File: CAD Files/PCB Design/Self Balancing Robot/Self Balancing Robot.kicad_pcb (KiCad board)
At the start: 2 copper layers, 82.5 x 53 mm, 17 parts, among them J1 Screw_Terminal_01x02, M1 Stepper_Motor_bipolar, M2 Stepper_Motor_bipolar, U1 DEVKIT_V1_ESP32-WROOM-32, U2 TSR_1-2450

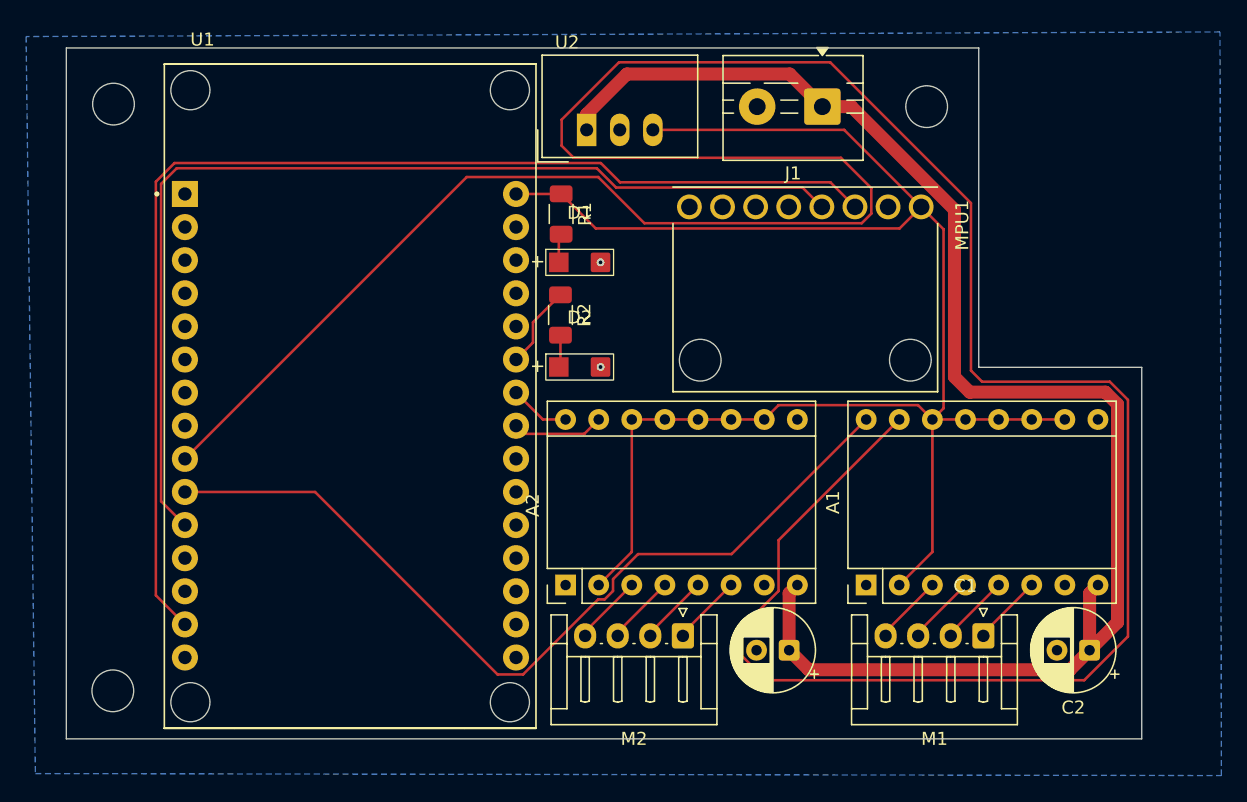
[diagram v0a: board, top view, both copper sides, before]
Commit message: Add 3d models
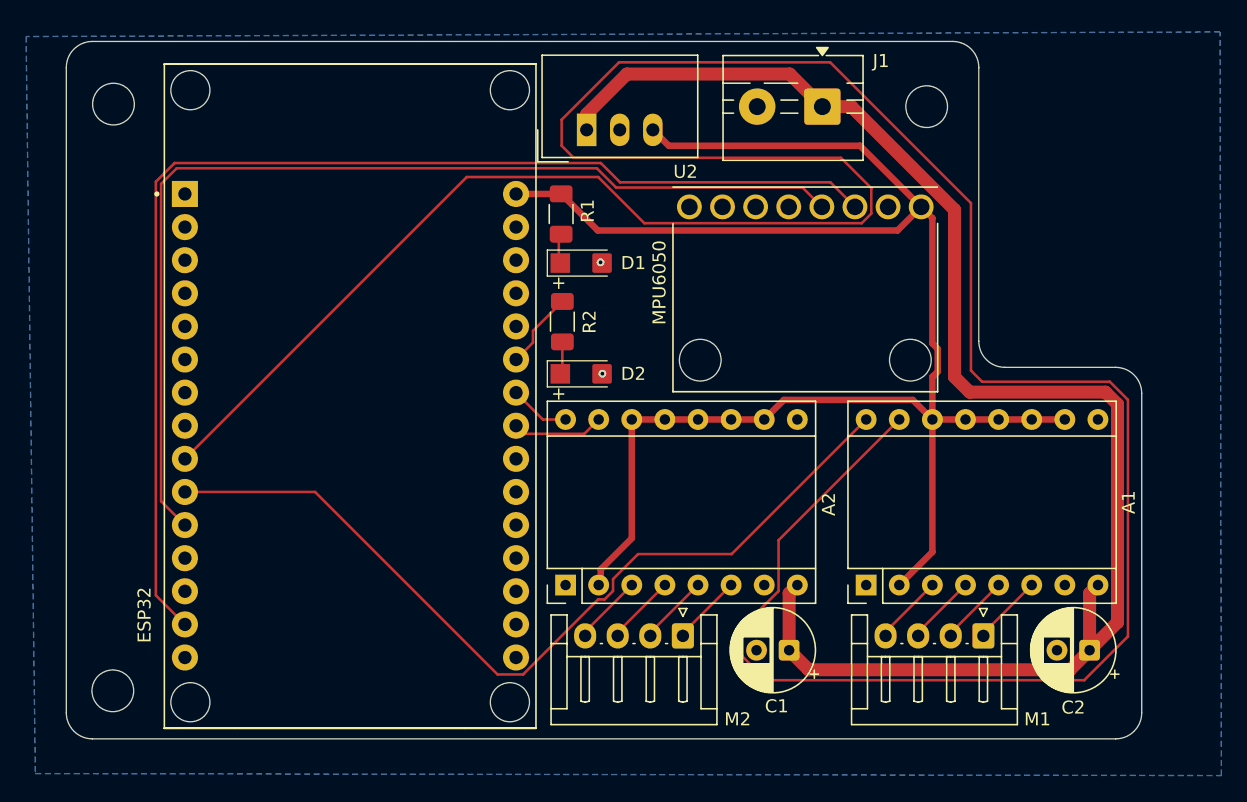
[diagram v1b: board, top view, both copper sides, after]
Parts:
- moved D2 0.54 mm to (126.0, 65.5)
- moved R2 0.53 mm to (124.6, 61.5)
- moved D1 0.13 mm to (126.0, 57.0)
- renumbered U1 to ESP32, MPU1 to MPU6050
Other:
- board size 82.5 x 53 mm -> 82.5 x 53.5 mm

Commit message: Update .gitignore to exclude additional KiCAD temporary files
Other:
- board text added: "Training Wheels v1"
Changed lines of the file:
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@@
 			(outputformat 1)
 			(mirror no)
-			(drillshape 1)
+			(drillshape 0)
 			(scaleselection 1)
-			(outputdirectory "")
+			(outputdirectory "./")
 		)
 	)
@@
 		(layer "Edge.Cuts")
 	)
+	(gr_text "Training Wheels v1"
+		(at 89.9668 70.3072 90)
+		(layer "F.SilkS")
+		(effects
+			(font
+				(size 1.5 1.5)
+				(thickness 0.3)
+				(bold yes)
+			)
+			(justify left bottom)
+		)
+	)
 	(segment
